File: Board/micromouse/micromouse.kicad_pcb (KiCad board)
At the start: 2 copper layers, 50 x 53 mm, 92 parts, among them J1 Conn_01x02_Pin, J2 Conn_02x03_Odd_Even, J3 Conn_01x06_Pin, J4 Conn_01x06_Pin, J5 Conn_01x06_Pin, J6 Conn_01x06_Pin, M1 Motor_DC, M2 Motor_DC, Q1 DMN63D8L-7, Q10 DMN63D8L-7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

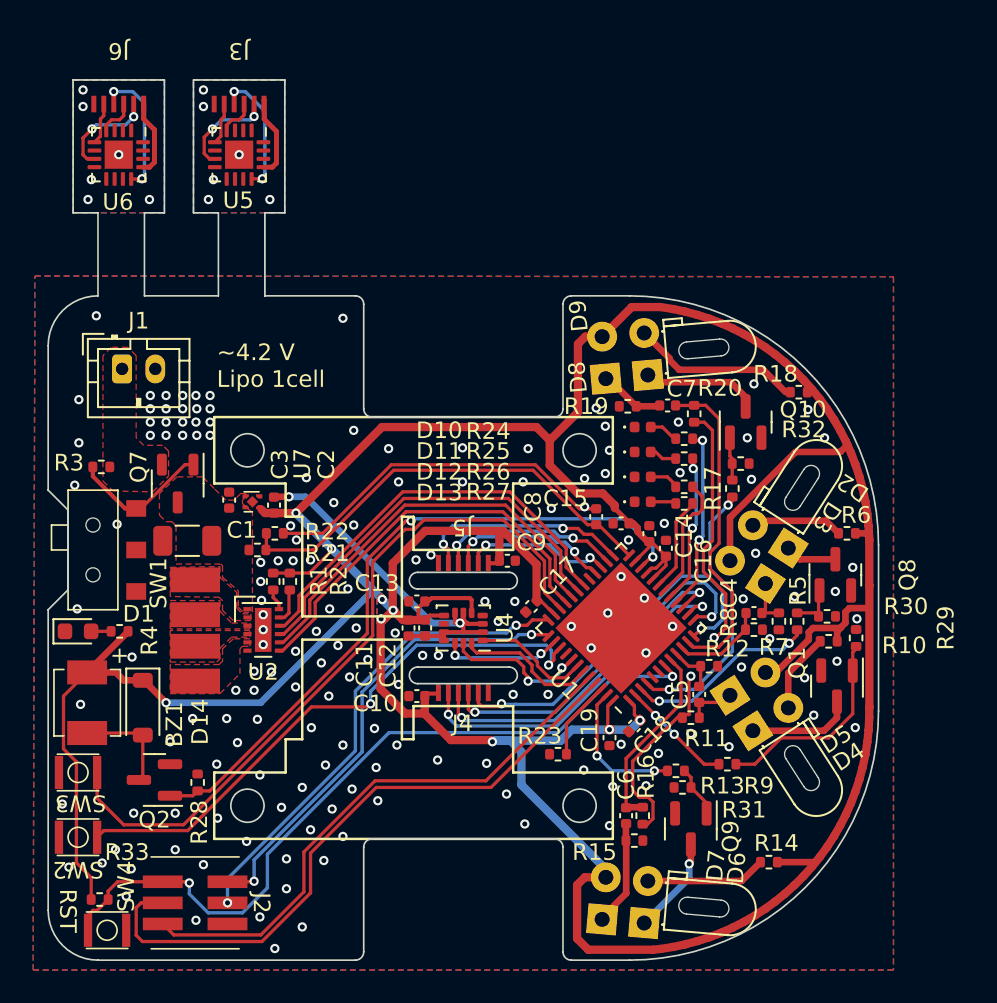
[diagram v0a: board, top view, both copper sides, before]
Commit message: ボタン位置修正
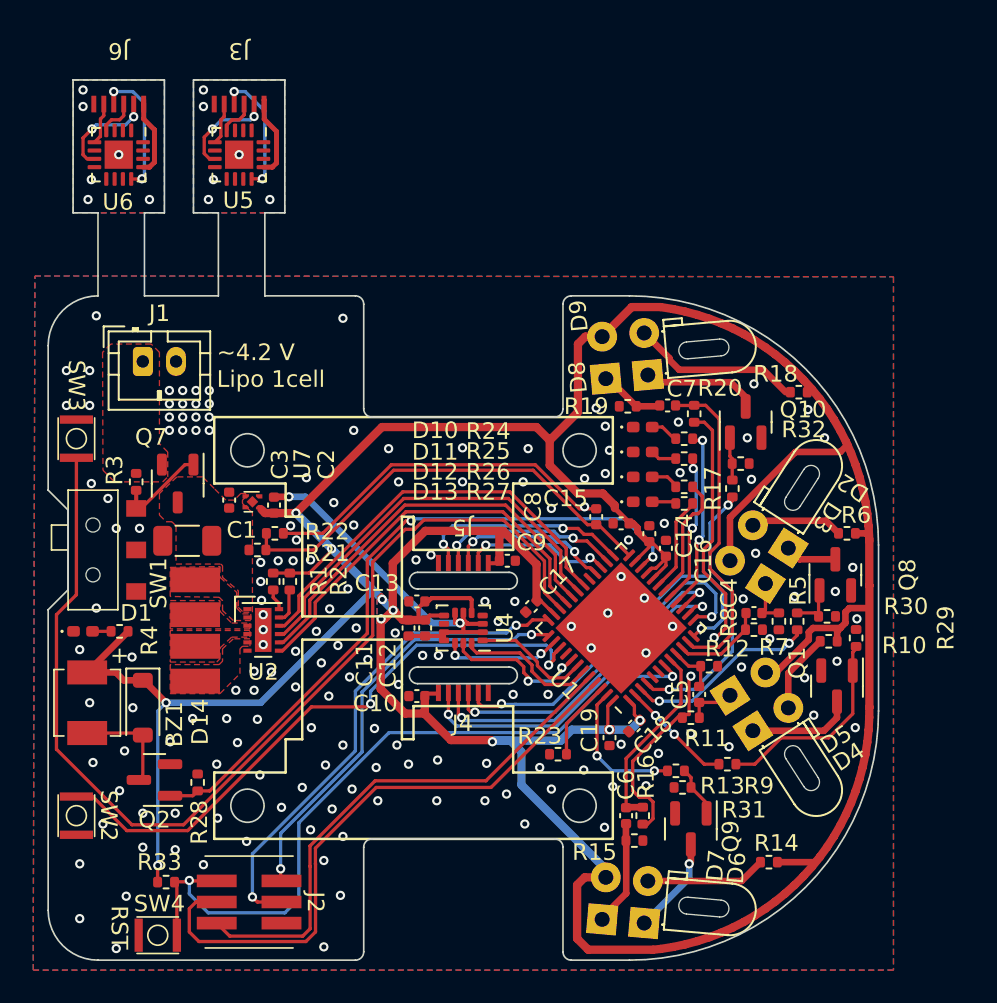
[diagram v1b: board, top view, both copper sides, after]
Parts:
- C4, C5, C6, C7: value 0.1u -> 0.01u
- D1: footprint LED_SMD:LED_0603_1608Metric -> LED_SMD:LED_0402_1005Metric_Pad0.77x0.64mm_HandSolder
- D10, D11, D12, D13: footprint LED_SMD:LED_0402_1005Metric -> LED_SMD:LED_0402_1005Metric_Pad0.77x0.64mm_HandSolder
- R24, R25, R26, R27, R4: value 1k -> 3.3k
- moved SW3 20.1 mm to (116.7, 88.6), turned to -90 degrees
- moved R33 4.14 mm to (122.1, 115.3)
- moved J2 3.25 mm to (127.1, 116.5)
- moved SW4 3.06 mm to (121.6, 118.5), turned to 0 degrees
- moved R3 2.28 mm to (120.3, 91.2), turned to -90 degrees
- moved J1 1.33 mm to (120.7, 84.0)
- moved SW2 1.30 mm to (116.7, 111.3), turned to 90 degrees
- moved D1 0.30 mm to (117.1, 100.2)
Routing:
- net /SW2: track 43.6 -> 63.8 mm
- net +3.3V: track 253.6 -> 249.7 mm, vias 9 -> 10
- net Net-(Q7-G): track 8.52 -> 5.63 mm
- net /SYS_JTMS-SWCLK: track 28.4 -> 26.1 mm
- net /SW1: track 35.0 -> 36.9 mm
- net /UART1_RX: track 39.0 -> 37.3 mm
- net /UART1_TX: track 33.8 -> 32.2 mm
- net /SYS_JTMS-SWDIO: track 29.3 -> 30.2 mm
- net /NRST: track 46.3 -> 45.5 mm
- net GND: track 71.6 -> 72.3 mm, vias 166 -> 172
